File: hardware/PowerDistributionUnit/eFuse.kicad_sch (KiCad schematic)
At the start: 25 parts, among them Q2 CSD18511Q5A, U4 AD5258, U5 TPS25983

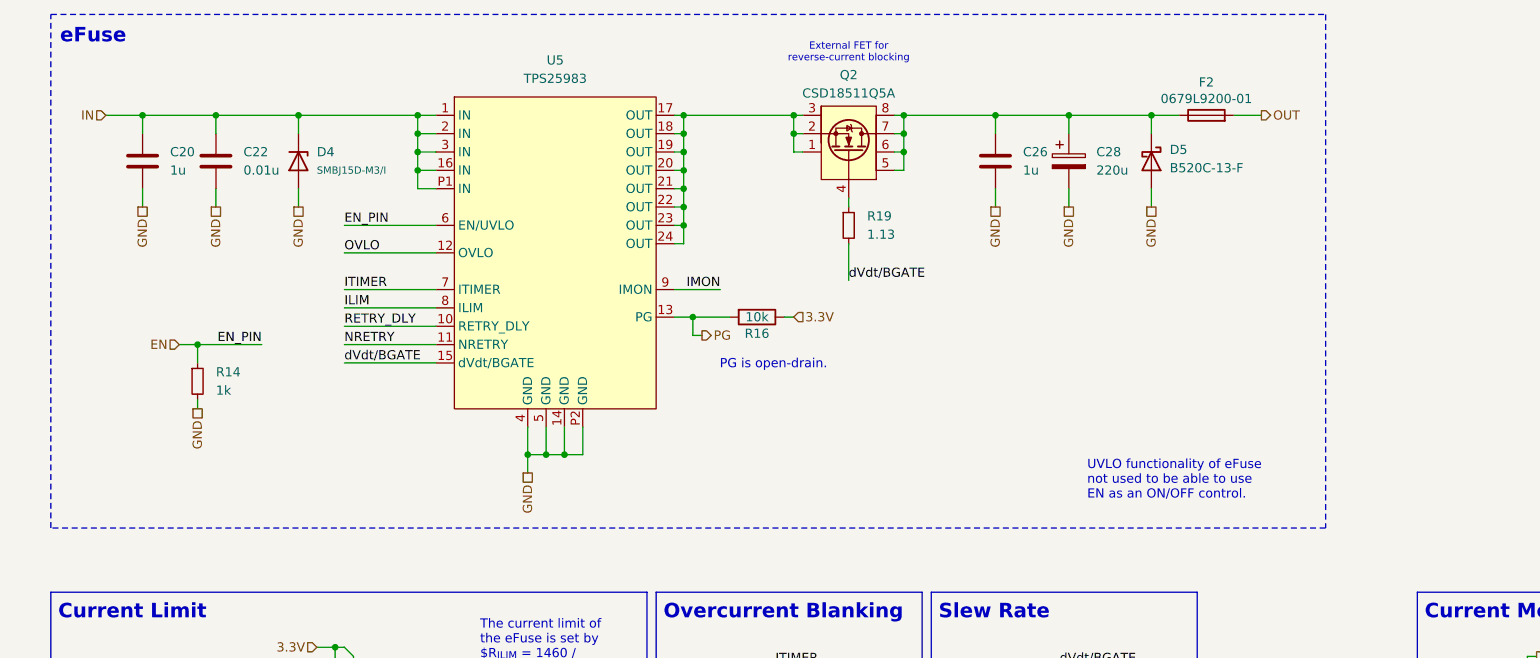
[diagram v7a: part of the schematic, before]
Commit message: added isolated CAN 5V DC-DC converter, updated power netclasses
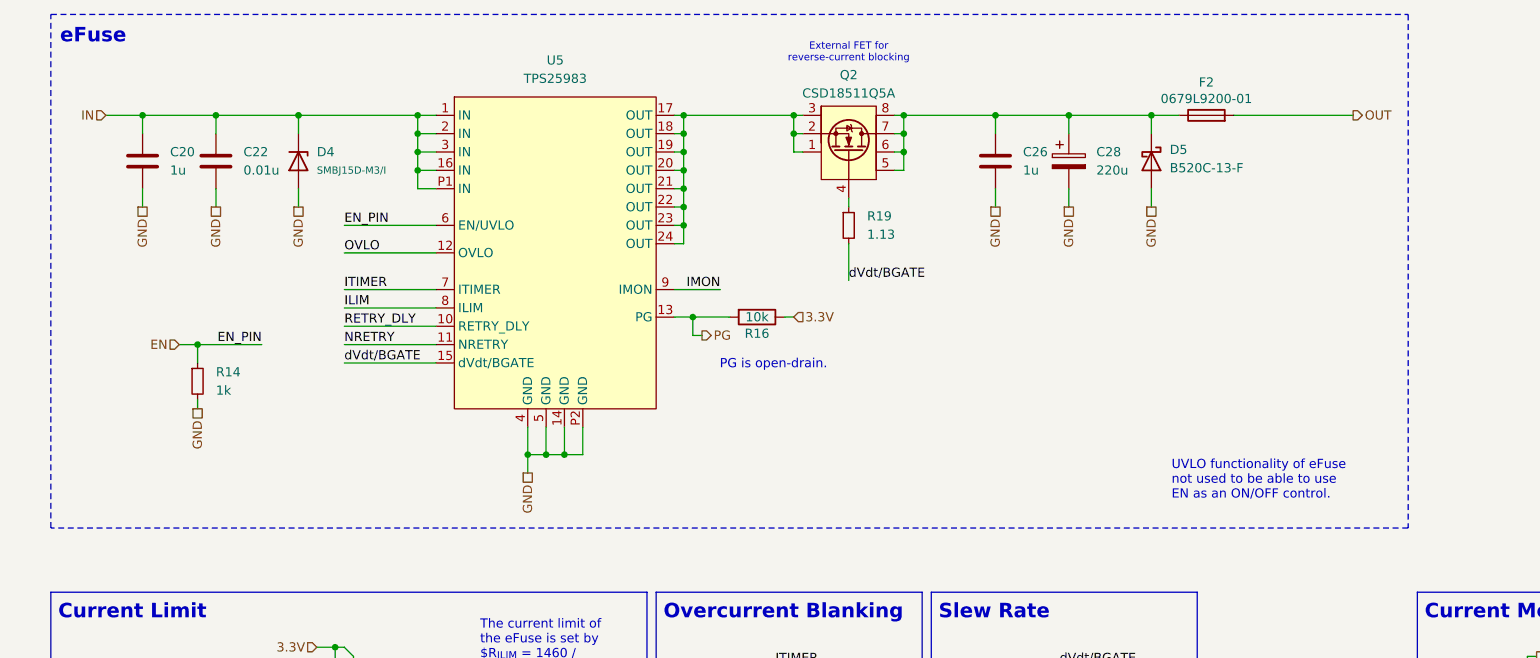
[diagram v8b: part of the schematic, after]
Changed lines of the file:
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@@
 	)
 	(junction
-		(at 30.48 34.29)
-		(diameter 0)
-		(color 0 0 0 0)
-	)
-	(junction
 		(at 83.82 81.28)
 		(diameter 0)
@@
 	)
 	(junction
+		(at 30.48 34.29)
+		(diameter 0)
+		(color 0 0 0 0)
+	)
+	(junction
 		(at 88.9 81.28)
 		(diameter 0)
@@
 	(wire
 		(pts
+			(xy 30.48 34.29) (xy 40.64 34.29)
+		)
+		(stroke
+			(width 0)
+			(type default)
+		)
+	)
+	(wire
+		(pts
 			(xy 52.07 34.29) (xy 68.58 34.29)
 		)
@@
 	(wire
 		(pts
+			(xy 25.4 34.29) (xy 30.48 34.29)
+		)
+		(stroke
+			(width 0)
+			(type default)
+		)
+	)
+	(wire
+		(pts
 			(xy 170.18 34.29) (xy 170.18 36.83)
 		)
@@
 	(wire
 		(pts
-			(xy 30.48 34.29) (xy 30.48 36.83)
-		)
-		(stroke
-			(width 0)
-			(type default)
-		)
-	)
-	(wire
-		(pts
 			(xy 157.48 120.65) (xy 157.48 123.19)
 		)
@@
 	(wire
 		(pts
-			(xy 30.48 34.29) (xy 40.64 34.29)
+			(xy 30.48 34.29) (xy 30.48 36.83)
 		)
 		(stroke
@@
 	(wire
 		(pts
-			(xy 25.4 34.29) (xy 30.48 34.29)
-		)
-		(stroke
-			(width 0)
-			(type default)
-		)
-	)
-	(wire
-		(pts
 			(xy 57.15 107.95) (xy 57.15 110.49)
 		)
@@
 	(wire
 		(pts
-			(xy 185.42 34.29) (xy 181.61 34.29)
+			(xy 198.12 34.29) (xy 181.61 34.29)
 		)
 		(stroke
@@
 	(rectangle
 		(start 17.78 20.32)
-		(end 194.31 91.44)
+		(end 205.74 91.44)
 		(stroke
 			(width 0)
@@
 	(text "UVLO functionality of eFuse\nnot used to be able to use \nEN as an ON/OFF control. "
 		(exclude_from_sim no)
-		(at 161.29 84.836 0)
+		(at 172.974 84.836 0)
 		(effects
 			(font
@@
 	(hierarchical_label "OUT"
 		(shape output)
-		(at 185.42 34.29 0)
+		(at 198.12 34.29 0)
 		(fields_autoplaced yes)
 		(effects
@@
 		(length 2.54)
 		(shape round)
-		(at 30.48 34.29 0)
+		(at 105.41 34.29 0)
 		(fields_autoplaced yes)
 		(effects
@@
 			(justify left bottom)
 		)
-		(property "Netclass" "HIGH POWER"
-			(at 31.1785 31.75 0)
+		(property "Netclass" "HIGH PWR"
+			(at 106.1085 31.75 0)
 			(effects
 				(font
@@
 		(length 2.54)
 		(shape round)
-		(at 105.41 34.29 0)
+		(at 186.69 34.29 0)
 		(fields_autoplaced yes)
 		(effects
@@
 			(justify left bottom)
 		)
-		(property "Netclass" "HIGH POWER"
-			(at 106.1085 31.75 0)
+		(property "Netclass" "HIGH PWR"
+			(at 187.3885 31.75 0)
+			(effects
+				(font
+					(size 1.27 1.27)
+					(italic yes)
+				)
+				(justify left)
+			)
+		)
+	)
+	(netclass_flag ""
+		(length 2.54)
+		(shape round)
+		(at 40.64 34.29 0)
+		(fields_autoplaced yes)
+		(effects
+			(font
+				(size 1.27 1.27)
+				(color 255 0 0 1)
+			)
+			(justify left bottom)
+		)
+		(property "Netclass" "HIGH PWR"
+			(at 41.3385 31.75 0)
 			(effects
 				(font
@@
 			(justify left bottom)
 		)
-		(property "Netclass" "HIGH POWER"
+		(property "Netclass" "HIGH PWR"
 			(at 136.5885 31.75 0)
 			(effects
